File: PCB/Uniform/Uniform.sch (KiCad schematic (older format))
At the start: 0 parts

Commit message: keyboard matrix schema finished
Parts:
- added D? (x68): D, symbol keyboard_parts:D
- added K_', K_,, K_-, K_., K_/, K_0, K_1, K_2, K_3, K_4, K_5, K_6, K_7, K_8, K_9, K_;, K_=, K_A, K_Alt, K_B, K_Backspace, K_C, K_Caps_Lock, K_Ctrl, K_D, K_Down, K_E, K_End, K_Enter, K_Esc, K_F, K_Fn0, K_Fn1, K_Fn2, K_Fn3, K_G, K_H, K_Home, K_I, K_J, K_K, K_L, K_LShift, K_LSpace, K_Left, K_M, K_N, K_O, K_P, K_Q, K_R, K_RShift, K_RSpace, K_Right, K_S, K_T, K_Tab, K_U, K_Up, K_V, K_W, K_Win, K_X, K_Y, K_Z, K_[, K_\, K_]: KEYSW, symbol keyboard_parts:KEYSW
- added U1: STM32F373CCT6, QFP50P900X900X160-48N, symbol STM32F373CCT6:STM32F373CCT6
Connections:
- new net: D?.2, K_Esc.2
- new net: D?.2, K_1.2
- new net: D?.2, K_2.2
- new net: D?.2, K_3.2
- new net: D?.2, K_4.2
- new net: D?.2, K_5.2
- new net: D?.2, K_6.2
- new net: D?.2, K_7.2
- new net: D?.2, K_8.2
- new net: D?.2, K_9.2
- new net: D?.2, K_0.2
- new net: D?.2, K_-.2
- new net: D?.2, K_=.2
- new net: D?.2, K_Tab.2
- new net: D?.2, K_Q.2
- new net: D?.2, K_W.2
- new net: D?.2, K_E.2
- new net: D?.2, K_R.2
- new net: D?.2, K_T.2
- new net: D?.2, K_Y.2
- new net: D?.2, K_U.2
- new net: D?.2, K_I.2
- new net: D?.2, K_O.2
- new net: D?.2, K_P.2
- new net: D?.2, K_[.2
- new net: D?.2, K_].2
- new net: D?.2, K_Caps_Lock.2
- new net: D?.2, K_A.2
- new net: D?.2, K_S.2
- new net: D?.2, K_D.2
- new net: D?.2, K_F.2
- new net: D?.2, K_G.2
- new net: D?.2, K_H.2
- new net: D?.2, K_J.2
- new net: D?.2, K_K.2
- new net: D?.2, K_L.2
- new net: D?.2, K_;.2
- new net: D?.2, K_'.2
- new net: D?.2, K_Enter.2
- new net: D?.2, K_LShift.2
- new net: D?.2, K_Z.2
- new net: D?.2, K_X.2
- new net: D?.2, K_C.2
- new net: D?.2, K_V.2
- new net: D?.2, K_B.2
- new net: D?.2, K_N.2
- new net: D?.2, K_M.2
- new net: D?.2, K_,.2
- new net: D?.2, K_..2
- new net: D?.2, K_/.2
- new net: D?.2, K_RShift.2
- new net: D?.2, K_Up.2
- new net: D?.2, K_Ctrl.2
- new net: D?.2, K_Win.2
- new net: D?.2, K_Alt.2
- new net: D?.2, K_LSpace.2
- new net: D?.2, K_Fn0.2
- new net: D?.2, K_RSpace.2
- new net: D?.2, K_Fn1.2
- new net: D?.2, K_Fn2.2
- new net: D?.2, K_Fn3.2
- new net: D?.2, K_Left.2
- new net: D?.2, K_Down.2
- new net: D?.2, K_Backspace.2
- new net: D?.2, K_\.2
- new net: D?.2, K_Home.2
- new net: D?.2, K_End.2
- new net: D?.2, K_Right.2
- new net C0: K_Caps_Lock.1, K_Ctrl.1, K_Esc.1, K_LShift.1, K_Tab.1
- new net C1: K_1.1, K_A.1, K_Q.1, K_Win.1, K_Z.1
- new net C10: K_/.1, K_0.1, K_;.1, K_Fn3.1, K_P.1
- new net C11: K_'.1, K_-.1, K_Left.1, K_RShift.1, K_[.1
- new net C12: K_=.1, K_Down.1, K_Enter.1, K_Up.1, K_].1
- new net C13: K_Backspace.1, K_End.1, K_Home.1, K_Right.1, K_\.1
- new net C2: K_2.1, K_Alt.1, K_S.1, K_W.1, K_X.1
- new net C3: K_3.1, K_C.1, K_D.1, K_E.1
- new net C4: K_4.1, K_F.1, K_LSpace.1, K_R.1, K_V.1
- new net C5: K_5.1, K_B.1, K_Fn0.1, K_G.1, K_T.1
- new net C6: K_6.1, K_H.1, K_N.1, K_RSpace.1, K_Y.1
- new net C7: K_7.1, K_J.1, K_M.1, K_U.1
- new net C8: K_,.1, K_8.1, K_Fn1.1, K_I.1, K_K.1
- new net C9: K_..1, K_9.1, K_Fn2.1, K_L.1, K_O.1
- new net R0: D?.1, D?.1, D?.1, D?.1, D?.1, D?.1, D?.1, D?.1, D?.1, D?.1, D?.1, D?.1, D?.1, D?.1
- new net R1: D?.1, D?.1, D?.1, D?.1, D?.1, D?.1, D?.1, D?.1, D?.1, D?.1, D?.1, D?.1, D?.1, D?.1
- new net R2: D?.1, D?.1, D?.1, D?.1, D?.1, D?.1, D?.1, D?.1, D?.1, D?.1, D?.1, D?.1, D?.1, D?.1
- new net R3: D?.1, D?.1, D?.1, D?.1, D?.1, D?.1, D?.1, D?.1, D?.1, D?.1, D?.1, D?.1, D?.1, D?.1
- new net R4: D?.1, D?.1, D?.1, D?.1, D?.1, D?.1, D?.1, D?.1, D?.1, D?.1, D?.1, D?.1

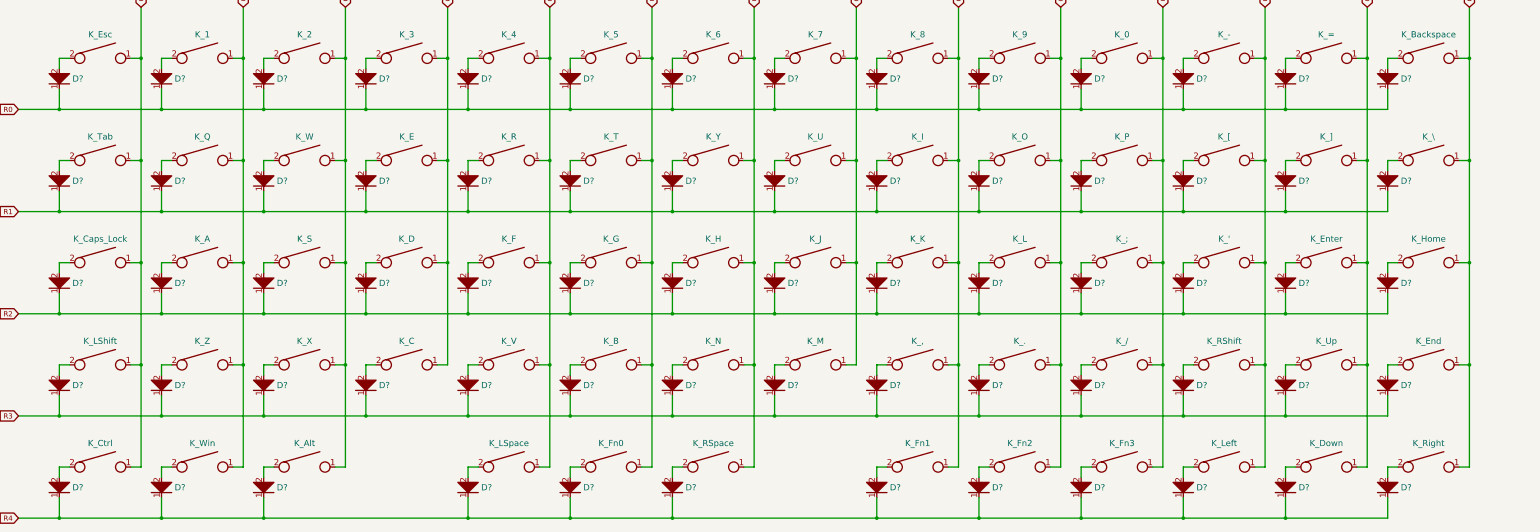
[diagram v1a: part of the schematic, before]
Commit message: added diode labels
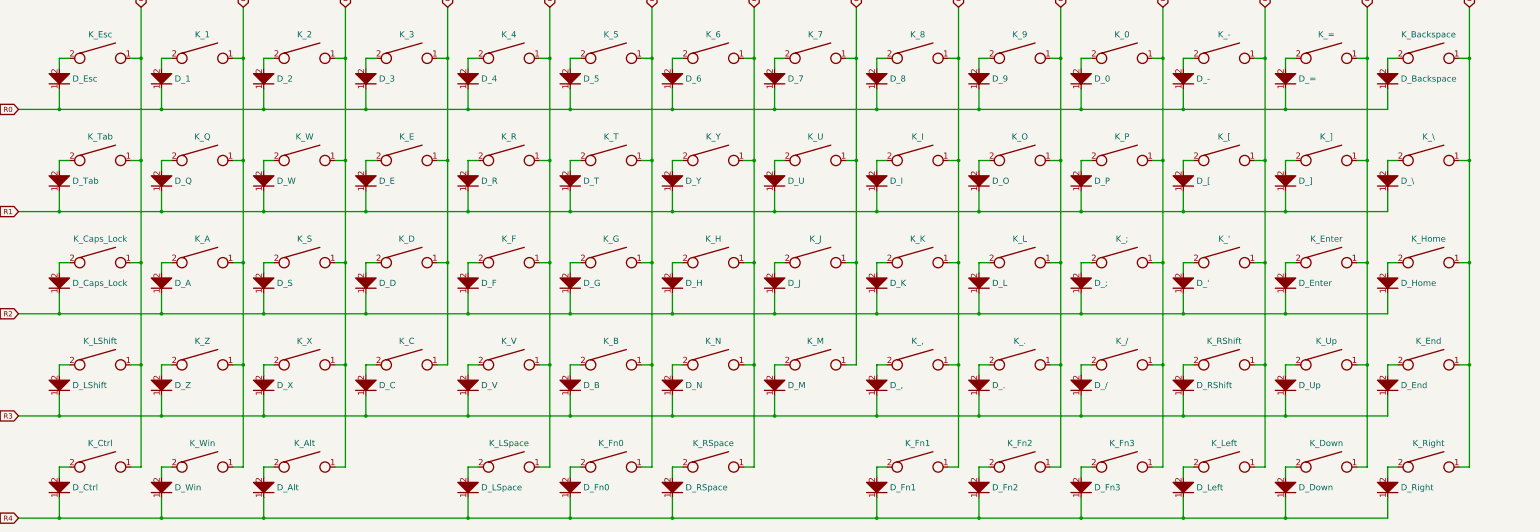
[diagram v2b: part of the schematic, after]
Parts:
- gave numbers to parts that had none: 68

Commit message: added crystal, voltage regulator, and boot/reset switches
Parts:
- added B_Boot, B_Reset, R1, R2: R, symbol Device:R
- added C1, C2: Capacitance??, symbol Device:C_Small
- added C3, C4: 10uf, symbol Device:C_Small
- added U2: TLV1117-33, symbol Regulator_Linear:TLV1117-33
- added X1: XTAL_GND, symbol keyboard_parts:XTAL_GND
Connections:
- net Boot: now reaches U1.44 (BOOT0)
- net Boot: now also B_Boot.2, R2.1
- net OSC_IN: now reaches U1.5 (PF0-OSC_IN)
- net OSC_IN: now also C1.1, X1.1
- net OSC_OUT: now reaches U1.6 (PF1-OSC_OUT)
- net OSC_OUT: now also C2.1, X1.2
- net Reset: now reaches U1.7 (NRST)
- net Reset: now also B_Reset.1, R1.2
- new net +3V3: B_Boot.1, C3.1, R1.1, U2.2 (VO)
- new net +5V: C4.1, U2.3 (VI)
- new net GND: B_Reset.2, C1.2, C2.2, R2.2, U2.1 (GND), X1.3
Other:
- moved on the sheet: D_', D_,, D_-, D_., D_/, D_0, D_1, D_2, D_3, D_4, D_5, D_6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

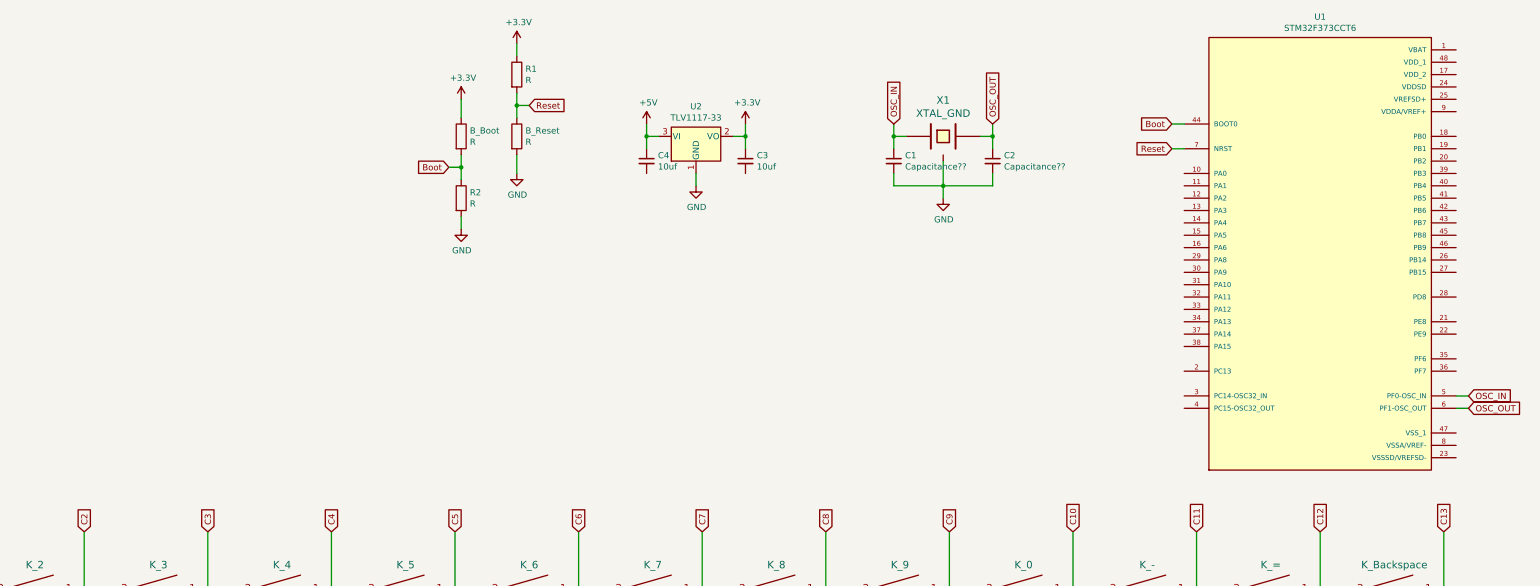
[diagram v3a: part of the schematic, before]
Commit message: added usb module to schema
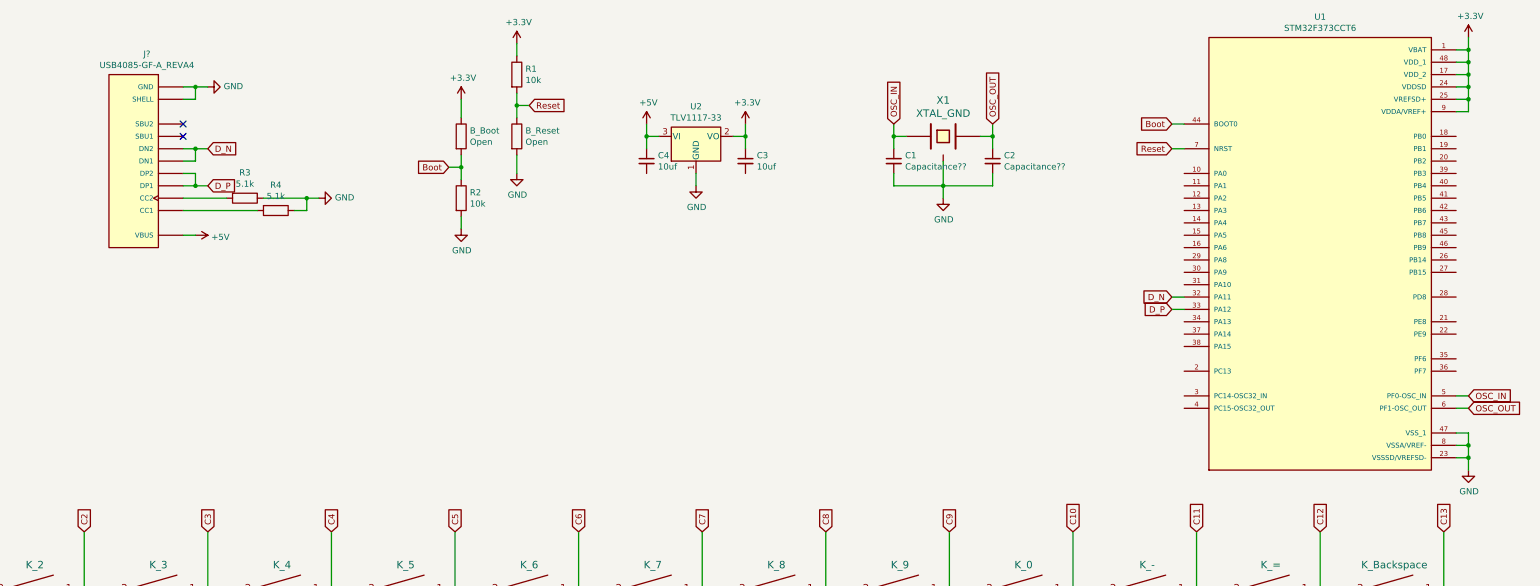
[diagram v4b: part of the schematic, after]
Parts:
- added J?: USB4085-GF-A_REVA4, GCT_USB4085-GF-A_REVA4, symbol USB4085-GF-A_REVA4:USB4085-GF-A_REVA4
- added R3, R4: 5.1k, symbol Device:R
- B_Boot, B_Reset: value R -> Open
- R1, R2: value R -> 10k
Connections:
- net +3V3: now also U1.1 (VBAT), U1.17 (VDD_2), U1.24 (VDDSD), U1.25 (VREFSD+), U1.48 (VDD_1), U1.9 (VDDA/VREF+)
- net +5V: now also J?.A4 (VBUS), J?.A9 (VBUS), J?.B4 (VBUS), J?.B9 (VBUS)
- net GND: now also U1.23 (VSSSD/VREFSD-), U1.47 (VSS_1), U1.8 (VSSA/VREF-), J?.A1 (GND), J?.A12 (GND), J?.B1 (GND), J?.B12 (GND), J?.P1 (SHELL), J?.P2 (SHELL), J?.P3 (SHELL), J?.P4 (SHELL), R3.1, R4.1
- net D_N: now reaches U1.32 (PA11)
- net D_N: now also J?.A7 (DN1), J?.B7 (DN2)
- net D_P: now reaches U1.33 (PA12)
- net D_P: now also J?.A6 (DP1), J?.B6 (DP2)
- new net: J?.A5 (CC1), R4.2
- new net: J?.B5 (CC2), R3.2
- no-connect marks 0 -> 2
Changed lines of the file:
@@
 P 7800 1500
 F 0 "B_Reset" H 7870 1546 50  0000 L CNN
-F 1 "R" H 7870 1455 50  0000 L CNN
+F 1 "Open" H 7870 1455 50  0000 L CNN
 F 2 "" V 7730 1500 50  0001 C CNN
 F 3 "~" H 7800 1500 50  0001 C CNN
@@
 P 7350 1500
 F 0 "B_Boot" H 7420 1546 50  0000 L CNN
-F 1 "R" H 7420 1455 50  0000 L CNN
+F 1 "Open" H 7420 1455 50  0000 L CNN
 F 2 "" V 7280 1500 50  0001 C CNN
 F 3 "~" H 7350 1500 50  0001 C CNN
@@
 P 7800 1000
 F 0 "R1" H 7870 1046 50  0000 L CNN
-F 1 "R" H 7870 955 50  0000 L CNN
+F 1 "10k" H 7870 955 50  0000 L CNN
 F 2 "" V 7730 1000 50  0001 C CNN
 F 3 "~" H 7800 1000 50  0001 C CNN
@@
 P 7350 2000
 F 0 "R2" H 7420 2046 50  0000 L CNN
-F 1 "R" H 7420 1955 50  0000 L CNN
+F 1 "10k" H 7420 1955 50  0000 L CNN
 F 2 "" V 7280 2000 50  0001 C CNN
 F 3 "~" H 7350 2000 50  0001 C CNN
@@
 Wire Wire Line
 	7350 1750 7350 1850
+$Comp
+L power:GND #PWR?
+U 1 1 63A346D9
+P 15500 4200
+F 0 "#PWR?" H 15500 3950 50  0001 C CNN
+F 1 "GND" H 15505 4027 50  0000 C CNN
+F 2 "" H 15500 4200 50  0001 C CNN
+F 3 "" H 15500 4200 50  0001 C CNN
+	1    15500 4200
+	1    0    0    -1
+$EndComp
+Wire Wire Line
+	15400 3900 15500 3900
+Wire Wire Line
+	15500 3900 15500 4000
+Wire Wire Line
+	15400 4000 15500 4000
+Connection ~ 15500 4000
+Wire Wire Line
+	15500 4000 15500 4100
+Wire Wire Line
+	15400 4100 15500 4100
+Connection ~ 15500 4100
+Wire Wire Line
+	15500 4100 15500 4200
+$Comp
+L power:+3.3V #PWR?
+U 1 1 63B37B64
+P 15500 700
+F 0 "#PWR?" H 15500 550 50  0001 C CNN
+F 1 "+3.3V" H 15515 873 50  0000 C CNN
+F 2 "" H 15500 700 50  0001 C CNN
+F 3 "" H 15500 700 50  0001 C CNN
+	1    15500 700
+	1    0    0    -1
+$EndComp
+Wire Wire Line
+	15400 1300 15500 1300
+Wire Wire Line
+	15500 1300 15500 1200
+Wire Wire Line
+	15400 1200 15500 1200
+Connection ~ 15500 1200
+Wire Wire Line
+	15500 1200 15500 1100
+Wire Wire Line
+	15400 1100 15500 1100
+Connection ~ 15500 1100
+Wire Wire Line
+	15500 1100 15500 1000
+Wire Wire Line
+	15400 1000 15500 1000
+Connection ~ 15500 1000
+Wire Wire Line
+	15500 1000 15500 900
+Wire Wire Line
+	15400 900  15500 900
+Connection ~ 15500 900
+Wire Wire Line
+	15500 900  15500 800
+Wire Wire Line
+	15400 800  15500 800
+Connection ~ 15500 800
+Wire Wire Line
+	15500 800  15500 700
+$Comp
+L USB4085-GF-A_REVA4:USB4085-GF-A_REVA4 J?
+U 1 1 63C7831B
+P 4700 1700
+F 0 "J?" H 4593 833 50  0000 C CNN
+F 1 "USB4085-GF-A_REVA4" H 4593 924 50  0000 C CNN
+F 2 "GCT_USB4085-GF-A_REVA4" H 4700 1700 50  0001 L BNN
+F 3 "" H 4700 1700 50  0001 L BNN
+F 4 "Manufacturer Recommendations" H 4700 1700 50  0001 L BNN "STANDARD"
+F 5 "3.46mm" H 4700 1700 50  0001 L BNN "MAXIMUM_PACKAGE_HEIGHT"
+F 6 "A4" H 4700 1700 50  0001 L BNN "PARTREV"
+F 7 "Global Connector Technology" H 4700 1700 50  0001 L BNN "MANUFACTURER"
+	1    4700 1700
+	-1   0    0    1
+$EndComp
+Text GLabel 5300 1600 2    50   Input ~ 0
+D_N
+Text GLabel 5300 1900 2    50   Input ~ 0
+D_P
+Wire Wire Line
+	5100 1900 5200 1900
+Wire Wire Line
+	5100 1800 5200 1800
+Wire Wire Line
+	5200 1800 5200 1900
+Connection ~ 5200 1900
+Wire Wire Line
+	5200 1900 5300 1900
+Wire Wire Line
+	5100 1600 5200 1600
+Wire Wire Line
+	5100 1700 5200 1700
+Wire Wire Line
+	5200 1700 5200 1600
+Connection ~ 5200 1600
+Wire Wire Line
+	5200 1600 5300 1600
+NoConn ~ 5100 1500
+NoConn ~ 5100 1400
+$Comp
+L power:GND #PWR?
+U 1 1 63DCA85F
+P 5300 1100
+F 0 "#PWR?" H 5300 850 50  0001 C CNN
+F 1 "GND" V 5305 972 50  0000 R CNN
+F 2 "" H 5300 1100 50  0001 C CNN
+F 3 "" H 5300 1100 50  0001 C CNN
+	1    5300 1100
+	0    -1   -1   0
+$EndComp
+Wire Wire Line
+	5100 1100 5200 1100
+Wire Wire Line
+	5100 1200 5200 1200
+Wire Wire Line
+	5200 1200 5200 1100
+Connection ~ 5200 1100
+Wire Wire Line
+	5200 1100 5300 1100
+$Comp
+L power:+5V #PWR?
+U 1 1 63E756A8
+P 5200 2300
+F 0 "#PWR?" H 5200 2150 50  0001 C CNN
+F 1 "+5V" V 5215 2428 50  0000 L CNN
+F 2 "" H 5200 2300 50  0001 C CNN
+F 3 "" H 5200 2300 50  0001 C CNN
+	1    5200 2300
+	0    1    1    0
+$EndComp
+Wire Wire Line
+	5100 2300 5200 2300
+$Comp
+L Device:R R3
+U 1 1 63EB21F8
+P 5600 2000
+F 0 "R3" V 5393 2000 50  0000 C CNN
+F 1 "5.1k" V 5484 2000 50  0000 C CNN
+F 2 "" V 5530 2000 50  0001 C CNN
+F 3 "~" H 5600 2000 50  0001 C CNN
+	1    5600 2000
+	0    1    1    0
+$EndComp
+$Comp
+L Device:R R4
+U 1 1 63EB4F24
+P 5850 2100
+F 0 "R4" V 5643 2100 50  0000 C CNN
+F 1 "5.1k" V 5734 2100 50  0000 C CNN
+F 2 "" V 5780 2100 50  0001 C CNN
+F 3 "~" H 5850 2100 50  0001 C CNN
+	1    5850 2100
+	0    1    1    0
+$EndComp
+$Comp
+L power:GND #PWR?
+U 1 1 63F64640
+P 6200 2000
+F 0 "#PWR?" H 6200 1750 50  0001 C CNN
+F 1 "GND" V 6205 1872 50  0000 R CNN
+F 2 "" H 6200 2000 50  0001 C CNN
+F 3 "" H 6200 2000 50  0001 C CNN
+	1    6200 2000
+	0    -1   -1   0
+$EndComp
+Wire Wire Line
+	6000 2100 6100 2100
+Wire Wire Line
+	6100 2100 6100 2000
+Wire Wire Line
+	6100 2000 6200 2000
+Wire Wire Line
+	6100 2000 5750 2000
+Connection ~ 6100 2000
+Wire Wire Line
+	5100 2000 5450 2000
+Wire Wire Line
+	5100 2100 5700 2100
+Text GLabel 13100 2900 0    50   Input ~ 0
+D_P
+Text GLabel 13100 2800 0    50   Input ~ 0
+D_N
+Wire Wire Line
+	13100 2800 13200 2800
+Wire Wire Line
+	13100 2900 13200 2900
 $EndSCHEMATC

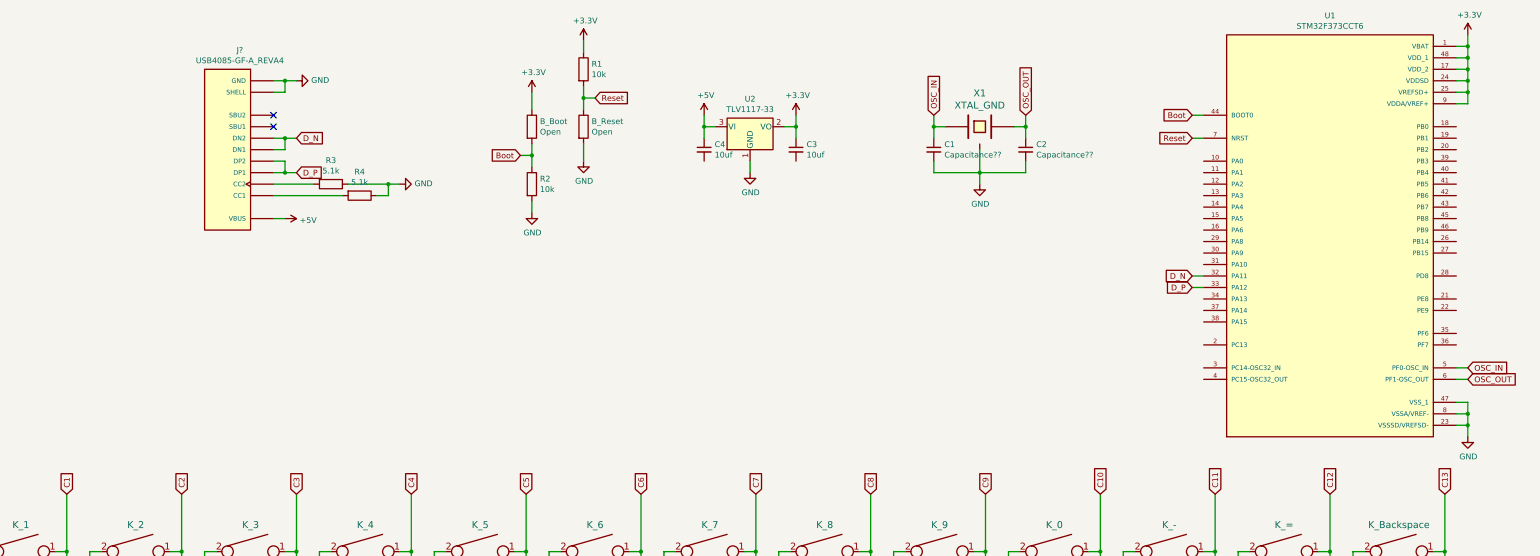
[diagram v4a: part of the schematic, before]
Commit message: mostly finished schema - need to select crystal and change flanking capacitor values accordingly
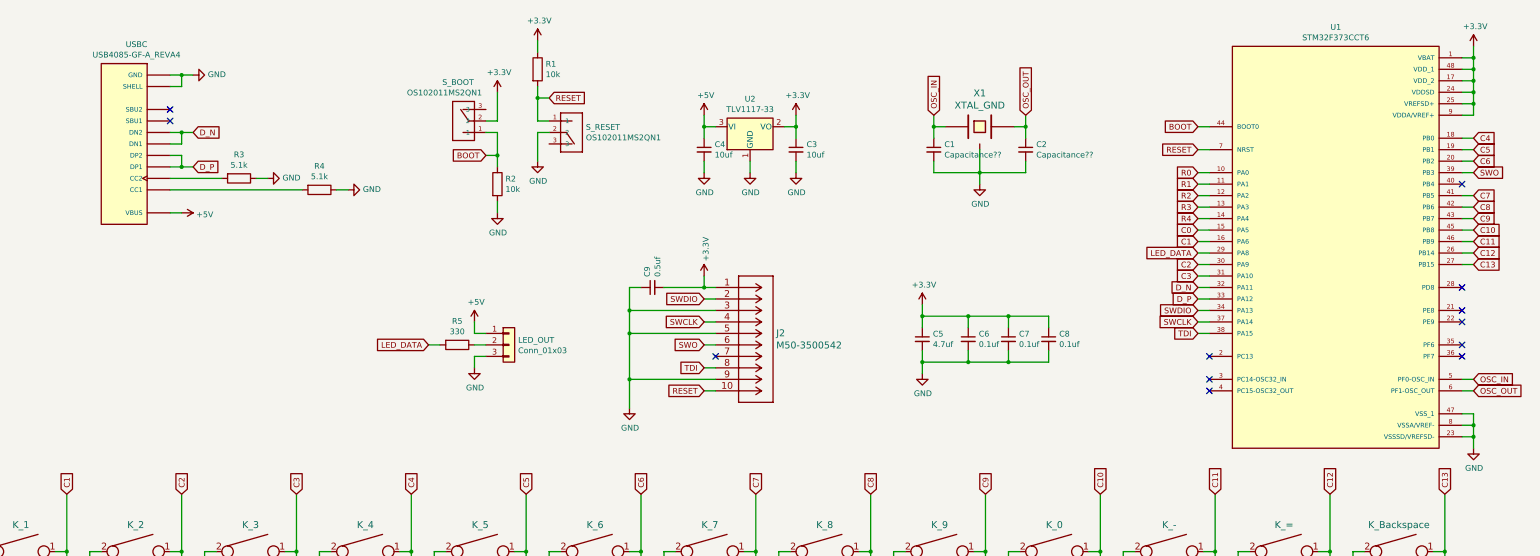
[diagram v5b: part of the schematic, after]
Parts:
- removed B_Boot, B_Reset: Open, symbol Device:R
- added C5: 4.7uf, symbol Device:C_Small
- added C6, C7, C8: 0.1uf, symbol Device:C_Small
- added C9: 0.5uf, symbol Device:C_Small
- added J2: M50-3500542, CONN10_500542_HRW, symbol ul_M50-3500542:M50-3500542
- added LED_OUT: Conn_01x03, symbol Connector_Generic:Conn_01x03
- added R5: 330, symbol Device:R
- added S_BOOT, S_RESET: OS102011MS2QN1, SW_OS102011MS2QN1, symbol OS102011MS2QN1:OS102011MS2QN1
- gave numbers to parts that had none: 1
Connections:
- net +3V3: now also C5.1, C6.1, C7.1, C8.1, C9.2, J2.1, S_BOOT.2
- net +5V: now also LED_OUT.1 (Pin_1)
- net C0: now also U1.15 (PA5)
- net C1: now also U1.16 (PA6)
- net C10: now also U1.45 (PB8)
- net C11: now also U1.46 (PB9)
- net C12: now also U1.26 (PB14)
- net C13: now also U1.27 (PB15)
- net C2: now also U1.30 (PA9)
- net C3: now also U1.31 (PA10)
- net C4: now also U1.18 (PB0)
- net C5: now also U1.19 (PB1)
- net C6: now also U1.20 (PB2)
- net C7: now also U1.41 (PB5)
- net C8: now also U1.42 (PB6)
- net C9: now also U1.43 (PB7)
- net GND: now also C3.2, C4.2, C5.2, C6.2, C7.2, C8.2, C9.1, J2.3, J2.5, J2.9, LED_OUT.3 (Pin_3), S_RESET.2
- net R0: now also U1.10 (PA0)
- net R1: now also U1.11 (PA1)
- net R2: now also U1.12 (PA2)
- net R3: now also U1.13 (PA3)
- net R4: now also U1.14 (PA4)
- net LED_DATA: now reaches U1.29 (PA8)
- net LED_DATA: now also R5.2
- net SWDIO: now reaches U1.34 (PA13)
- net SWDIO: now also J2.2
- net SWCLK: now reaches U1.37 (PA14)
- net SWCLK: now also J2.4
- net TDI: now reaches U1.38 (PA15)
- net TDI: now also J2.8
- net SWO: now reaches U1.39 (PB3)
- net SWO: now also J2.6
- net Boot renamed BOOT
- net BOOT: now also S_BOOT.1
- net Reset renamed RESET
- net RESET: now also J2.10, S_RESET.1
- new net: LED_OUT.2 (Pin_2), R5.1
- no-connect marks 2 -> 12
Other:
- moved on the sheet: R1, R2, R3, R4, U1, USBC
